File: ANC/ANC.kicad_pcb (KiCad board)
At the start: 2 copper layers, 72.9 x 41.9 mm, 83 parts, among them J1 Screw_Terminal_01x04, J10 Conn_01x03, J11 Conn_01x03, J12 Conn_01x03, J13 Conn_01x03, J2 Screw_Terminal_01x02, J3 SJ2-35894B-SMT-TR, J4 Conn_01x04, J5 Conn_01x04, J6 Conn_01x06, J7 Conn_01x04, J8 Conn_01x04, J9 Conn_01x04, U1 ICS-40730, U10 LD39015M12R, U2 MAX98090AETL_T, U3 ICS-40730, U4 CMM-3729AB-38308-TR, U5 CMM-3729AB-38308-TR, U6 TLV172IDCK, U7 TLV172IDCK, U8 LD1117S12TR_SOT223, U9 LD39015M18R, Y1 ASE-12.288MHZ-LC-T

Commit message: Updated ANC.
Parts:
- moved C11 1.29 mm to (147.3, 90.8), turned to -90 degrees
- moved C1 0.33 mm to (143.0, 86.4), turned to 180 degrees
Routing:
- net 3.3V: track 165.6 -> 177.6 mm, vias 6 -> 12
- net VDD: track 89.6 -> 91.5 mm, vias 8 -> 10
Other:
- board size 72.9 x 41.9 mm -> 73.3 x 42.5 mm

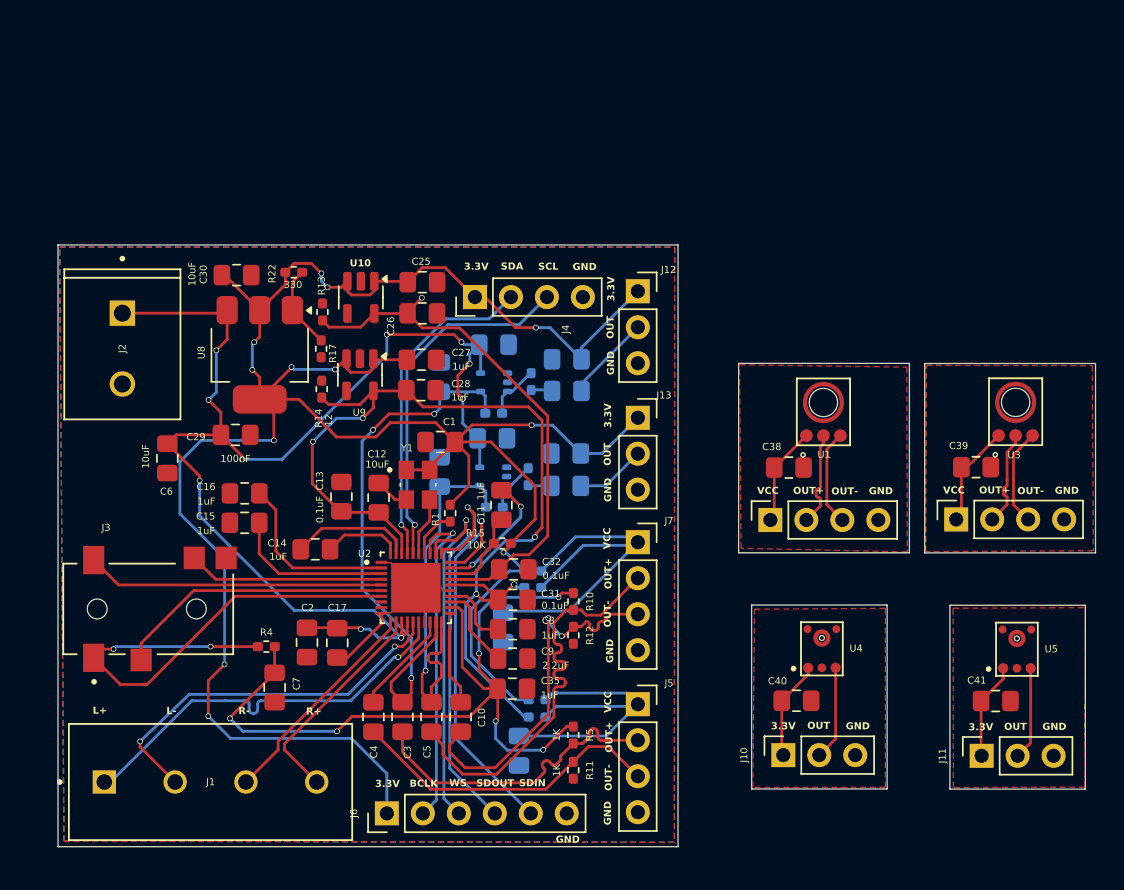
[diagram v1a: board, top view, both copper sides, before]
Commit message: Added ANC
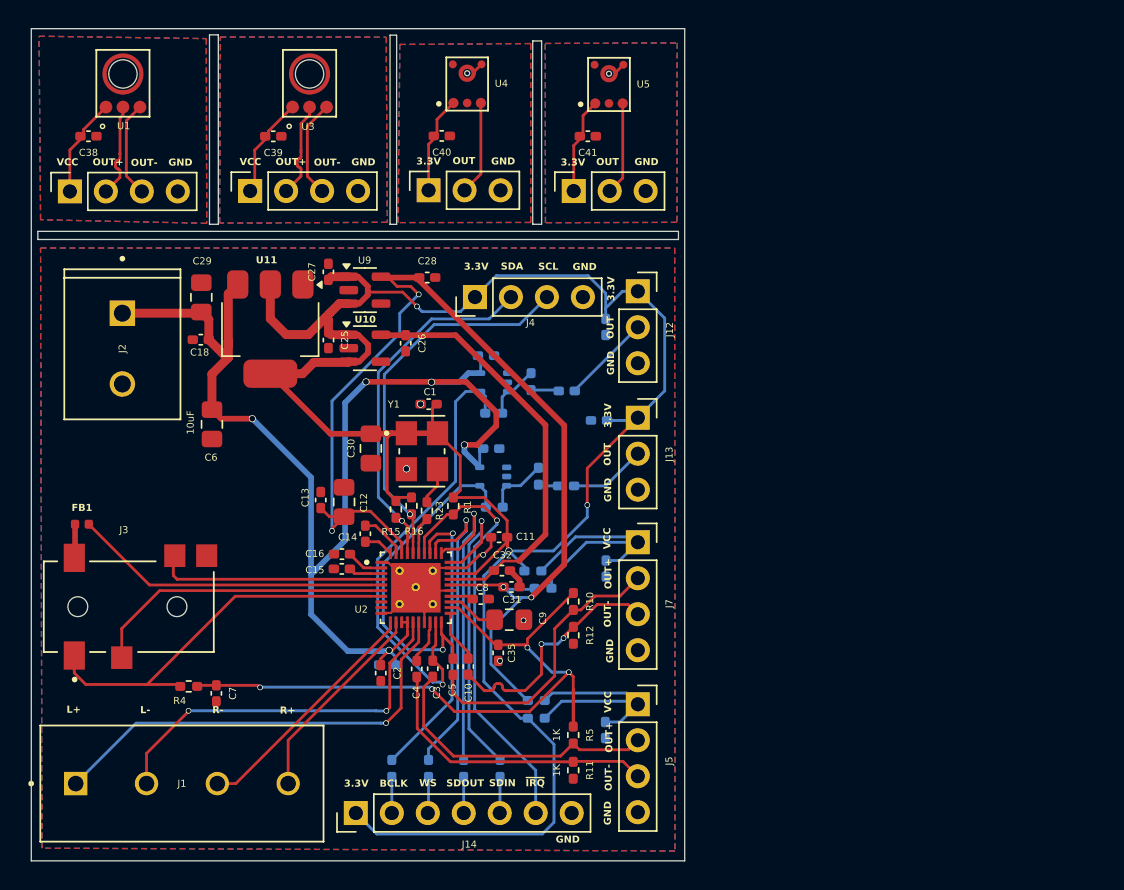
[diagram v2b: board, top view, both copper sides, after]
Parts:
- removed C23, C24: 0.1uF, Capacitor_SMD:C_0805_2012Metric_Pad1.18x1.45mm_HandSolder
- removed J6: Conn_01x06, Connector_PinHeader_2.54mm:PinHeader_1x06_P2.54mm_Vertical
- removed the R13 at (134.7, 77.2)
- removed the R14 at (134.6, 82.6)
- removed R17: 541, Resistor_SMD:R_0402_1005Metric_Pad0.72x0.64mm_HandSolder
- removed R22: 330, Resistor_SMD:R_0402_1005Metric_Pad0.72x0.64mm_HandSolder
- removed U8: LD1117S12TR_SOT223, Package_TO_SOT_SMD:SOT-223-3_TabPin2
- added C18: 0.1uF, Capacitor_SMD:C_0402_1005Metric_Pad0.74x0.62mm_HandSolder, F.Cu at (126.1, 79.2)
- added FB1: FerriteBead, Inductor_SMD:L_0402_1005Metric, F.Cu at (117.7, 92.2)
- added J14: Conn_01x07, Connector_PinHeader_2.54mm:PinHeader_1x07_P2.54mm_Vertical, F.Cu at (137.0, 112.6)
- added R16: 10K, Resistor_SMD:R_0402_1005Metric_Pad0.72x0.64mm_HandSolder, F.Cu at (140.9, 90.9)
- added R18: 22, Resistor_SMD:R_0402_1005Metric_Pad0.72x0.64mm_HandSolder, B.Cu at (139.6, 109.4)
- added R19: 22, Resistor_SMD:R_0402_1005Metric_Pad0.72x0.64mm_HandSolder, B.Cu at (142.1, 109.4)
- added R20: 22, Resistor_SMD:R_0402_1005Metric_Pad0.72x0.64mm_HandSolder, B.Cu at (144.6, 109.4)
- added R21: 22, Resistor_SMD:R_0402_1005Metric_Pad0.72x0.64mm_HandSolder, B.Cu at (147.2, 109.4)
- added R23: 22, Resistor_SMD:R_0402_1005Metric_Pad0.72x0.64mm_HandSolder, F.Cu at (142.0, 91.2)
- added U11: LD1117S33TR_SOT223, Package_TO_SOT_SMD:SOT-223-3_TabPin2, F.Cu at (131.0, 78.4)
- C1, C10, C11, C13, C14, C15, C16, C19, C2, C20, C21, C22, C25, C26, C27, C28, C3, C33, C34, C35, C36, C37, C4, C5, C7, C8: footprint Capacitor_SMD:C_0805_2012Metric_Pad1.18x1.45mm_HandSolder -> Capacitor_SMD:C_0402_1005Metric_Pad0.74x0.62mm_HandSolder
- C17: footprint Capacitor_SMD:C_0805_2012Metric_Pad1.18x1.45mm_HandSolder -> Capacitor_SMD:C_0402_1005Metric_Pad0.74x0.62mm_HandSolder; moved to B.Cu
- C29: value 100nF -> 47uF
- C31, C32: value 0.1uF -> 1uF; footprint Capacitor_SMD:C_0805_2012Metric_Pad1.18x1.45mm_HandSolder -> Capacitor_SMD:C_0402_1005Metric_Pad0.74x0.62mm_HandSolder
- C38, C39, C40, C41: value 0.1u -> 0.1uF; footprint Capacitor_SMD:C_0805_2012Metric_Pad1.18x1.45mm_HandSolder -> Capacitor_SMD:C_0402_1005Metric_Pad0.74x0.62mm_HandSolder
- R13, R14, R8, R9: renamed from no load
- Y1: value ASE-12.288MHZ-LC-T -> ASFL1-12.288MHZ-EC-T; footprint ASE-12.288MHZ-LC-T:XTAL_ASE-12.288MHZ-LC-T -> ASFL1_12_288MHZ_EC_T:XTAL_ASFL1-12.288MHZ-EC-T
- moved J9 55.0 mm to (129.5, 68.7)
- moved U3 55.0 mm to (133.7, 61.0)
- moved C39 54.8 mm to (131.2, 64.8)
- moved C38 54.7 mm to (118.1, 64.8)
- moved J8 54.6 mm to (116.8, 68.7)
- moved U1 54.6 mm to (120.6, 61.0)
- moved C41 49.2 mm to (153.4, 64.8)
- moved U5 49.2 mm to (154.9, 61.1)
- moved J11 49.2 mm to (152.4, 68.7)
- moved C40 47.1 mm to (143.1, 64.8)
- moved J10 47.1 mm to (142.1, 68.6)
- moved U4 47.1 mm to (144.9, 61.1)
- moved C30 15.5 mm to (138.1, 86.8), turned to -90 degrees
- moved C29 10.0 mm to (126.1, 76.2), turned to 90 degrees
- moved C27 9.04 mm to (135.1, 74.4), turned to 90 degrees
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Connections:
- C11 pad 1: /DGND -> GND
- C11 pad 2: Net-(U2-DVDDIO) -> 3.3V
- J3 pad 4: /HPSNS -> GND
- R15 pad 2: Net-(U2-DVDDIO) -> /SDA
- U2 pad 28: Net-(U2-DVDDIO) -> 3.3V
- U2 pad 29: /DGND -> GND
- U2 pad 5: /HPSNS -> Net-(U2-HPSNS)
- Y1 pad 3: /MCLK -> Net-(Y1-OUTPUT)
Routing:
- net /~{IRQ}: track 3.40 -> 30.7 mm, vias 0 -> 1
- net Net-(U2-HPSNS): track 0.00 -> 22.4 mm
- net /HPSNS: track 21.0 -> 0.00 mm
- net 3.3V: track 177.6 -> 157.1 mm, vias 12 -> 3
- net Net-(U2-CPVSS): track 12.7 -> 2.62 mm
- net 1.8V: track 69.9 -> 79.2 mm, vias 6 -> 4
- net Net-(U2-CPVDD): track 11.7 -> 2.36 mm
- net /DGND: track 9.22 -> 0.00 mm, vias 2 -> 0
- net /OUTPUT-: track 26.1 -> 17.1 mm
- net /OUTPUT+: track 29.1 -> 20.2 mm
- net /ICS_VDD: track 27.7 -> 18.9 mm
- net /MICBIAS: track 58.6 -> 50.4 mm, vias 6 -> 4
- net 1.2V: track 37.9 -> 30.0 mm, vias 1 -> 0
- net /JACKSNS: track 35.6 -> 28.3 mm, vias 2 -> 0
- net /SDOUT: track 28.8 -> 22.1 mm
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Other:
- board size 73.3 x 42.5 mm -> 46.1 x 58.8 mm
- board text added: "~{IRQ}"
